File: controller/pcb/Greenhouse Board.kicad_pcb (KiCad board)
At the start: 2 copper layers, 29.1 x 55.5 mm, 9 parts, among them J1 window_control, J2 fan_control, J3 temp_humidity_sensor, J4 misc_sensor_1, J5 misc_sensor_2, Q1 Q_NMOS_GDS, Q2 Q_NMOS_GDS, U1 ESP32-DEVKITC-32D

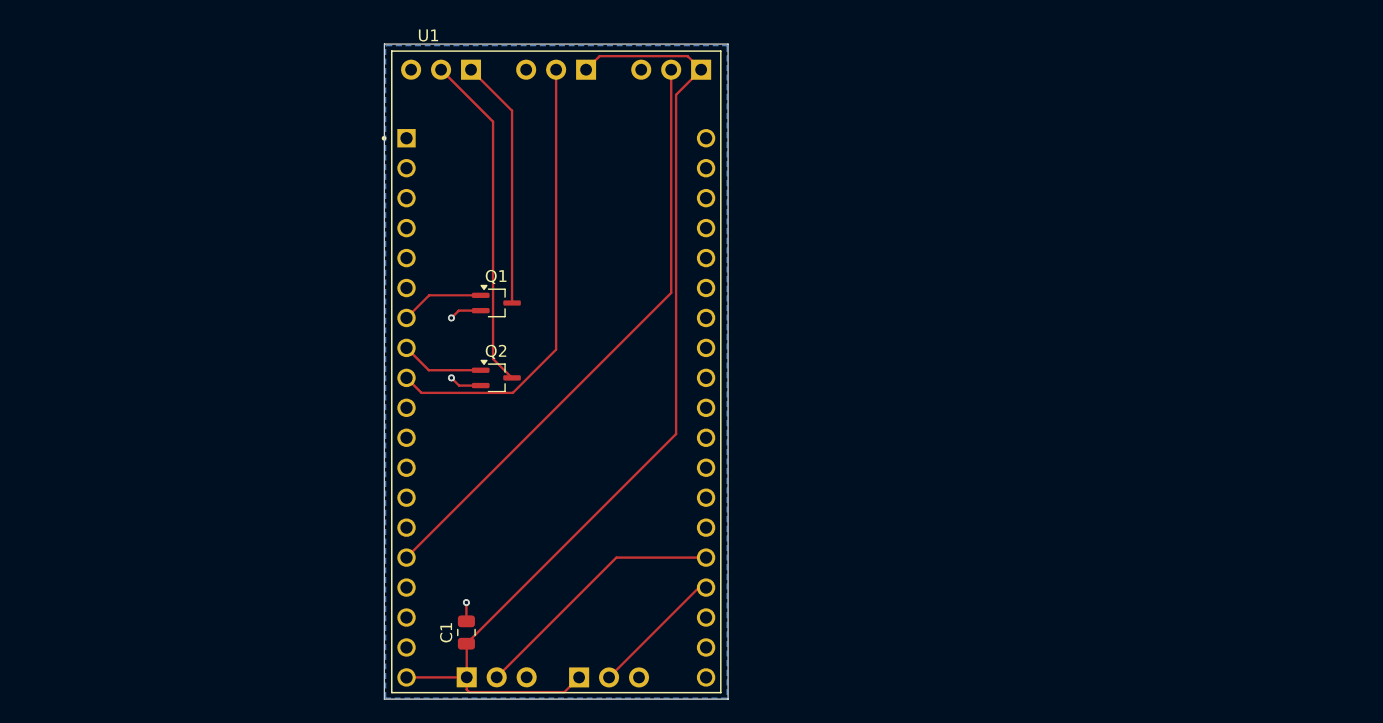
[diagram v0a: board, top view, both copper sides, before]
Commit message: Updates to the PCB to expand its inputs/outputs
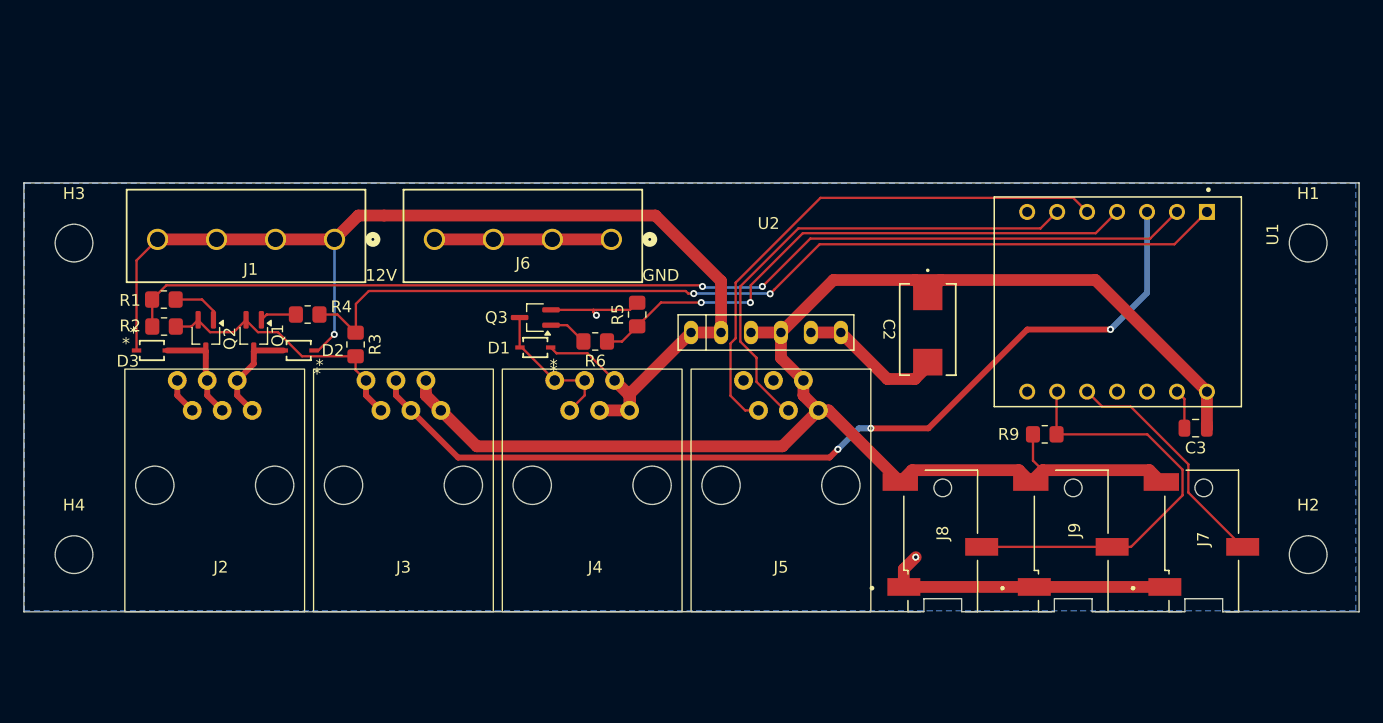
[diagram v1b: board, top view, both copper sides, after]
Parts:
- removed C1: C, Capacitor_SMD:C_0805_2012Metric
- added C2: 220u, Garth:CAP_SP-CAP_SR_PAN, F.Cu at (172.5, 89.9)
- added C3: .1u, Capacitor_SMD:C_0805_2012Metric, F.Cu at (195.2, 98.2)
- added D1: D, Garth:SOD323_DIO, F.Cu at (139.2, 91.4)
- added D2: D, Garth:SOD323_DIO, F.Cu at (119.1, 91.7)
- added D3: D, Garth:SOD323_DIO, F.Cu at (106.7, 91.7)
- added H1: MountingHole, MountingHole:MountingHole_3.2mm_M3, F.Cu at (204.7, 82.5)
- added H2: MountingHole, MountingHole:MountingHole_3.2mm_M3, F.Cu at (204.7, 109.0)
- added H3: MountingHole, MountingHole:MountingHole_3.2mm_M3, F.Cu at (100.1, 82.5)
- added H4: MountingHole, MountingHole:MountingHole_3.2mm_M3, F.Cu at (100.1, 109.0)
- added J6: GND, Garth:screw-terminal-CONN4_TB002-500_787x299_CUD, F.Cu at (145.6, 82.2)
- added J7: T+H sensor, Garth:1_8jack-CUI_SJ2-35853A-SMT-TR, F.Cu at (195.9, 107.8)
- added J8: temp sensor 1, Garth:1_8jack-CUI_SJ2-35853A-SMT-TR, F.Cu at (173.7, 107.8)
- added J9: temp sensor 2, Garth:1_8jack-CUI_SJ2-35853A-SMT-TR, F.Cu at (184.8, 107.8)
- added Q3: Q_NMOS_GDS, Package_TO_SOT_SMD:SOT-323_SC-70_Handsoldering, F.Cu at (139.2, 88.9)
- added R1: 1k, Resistor_SMD:R_0805_2012Metric_Pad1.20x1.40mm_HandSolder, F.Cu at (107.7, 87.3)
- added R2: 100k, Resistor_SMD:R_0805_2012Metric_Pad1.20x1.40mm_HandSolder, F.Cu at (107.7, 89.6)
- added R3: 100k, Resistor_SMD:R_0805_2012Metric_Pad1.20x1.40mm_HandSolder, F.Cu at (124.0, 91.1)
- added R4: 1k, Resistor_SMD:R_0805_2012Metric_Pad1.20x1.40mm_HandSolder, F.Cu at (119.9, 88.6)
- added R5: 100k, Resistor_SMD:R_0805_2012Metric_Pad1.20x1.40mm_HandSolder, F.Cu at (147.8, 88.6)
- added R6: 1k, Resistor_SMD:R_0805_2012Metric_Pad1.20x1.40mm_HandSolder, F.Cu at (144.3, 90.9)
- added R9: 100k, Resistor_SMD:R_0805_2012Metric_Pad1.20x1.40mm_HandSolder, F.Cu at (182.4, 98.8)
- added U2: 12-5V DC/DC, Garth:Power Module 6-pin, F.Cu at (150.5, 92.0)
- J1: value window_control -> 12V; footprint Connector_PinSocket_2.54mm:PinSocket_1x03_P2.54mm_Vertical -> Garth:screw-terminal-CONN4_TB002-500_787x299_CUD; moved to F.Cu
- J2: value fan_control -> window control; footprint Connector_PinSocket_2.54mm:PinSocket_1x03_P2.54mm_Vertical -> Garth:RJ11-RA; moved to F.Cu
- J3: value temp_humidity_sensor -> fan control; footprint Connector_PinSocket_2.54mm:PinSocket_1x03_P2.54mm_Vertical -> Garth:RJ11-RA; moved to F.Cu
- J4: value misc_sensor_1 -> misting control; footprint Connector_PinSocket_2.54mm:PinSocket_1x03_P2.54mm_Vertical -> Garth:RJ11-RA; moved to F.Cu
- J5: value misc_sensor_2 -> light_sensor; footprint Connector_PinSocket_2.54mm:PinSocket_1x03_P2.54mm_Vertical -> Garth:RJ11-RA; moved to F.Cu
- U1: value ESP32-DEVKITC-32D -> XAIO ESP32-C3; footprint ESP32-DEVKITC-32D:MODULE_ESP32-DEVKITC-32D -> Garth:MODULE_113991054
- moved U1 48.0 mm to (188.6, 87.5), turned to -90 degrees
- moved J2 42.7 mm to (112.0, 96.7), turned to 180 degrees
- moved J3 38.4 mm to (128.0, 96.7), turned to 180 degrees
- moved J5 28.4 mm to (160.0, 96.7), turned to 180 degrees
- moved J4 25.0 mm to (144.0, 96.7), turned to 180 degrees
- moved Q2 24.9 mm to (111.3, 90.4), turned to -90 degrees
- moved Q1 20.8 mm to (115.3, 90.4), turned to -90 degrees
- moved J1 18.5 mm to (122.2, 82.2), turned to 0 degrees
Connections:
- J1 pad 1: /green_wire -> +12V
- J1 pad 2: /red_wire -> +12V
- J1 pad 3: GND -> +12V
- J2 pad 1: +5V -> /green_wire
- J2 pad 2: /fan_signal -> /green_wire
- J2 pad 3: GND -> /red_wire
- J3 pad 2: /temp_data -> +5V
- J3 pad 3: GND -> /fan_signal
- J4 pad 1: +5V -> +12V
- J4 pad 2: /misc_data1 -> +12V
- J4 pad 3: GND -> +12V
- J5 pad 2: /misc_data2 -> +5V
- J5 pad 3: GND -> /SCL
- Q1 pad 1: /window_close -> Net-(Q1-G)
- Q2 pad 1: /window_open -> Net-(Q2-G)
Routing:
- net +12V: track 0.00 -> 99.3 mm, vias 0 -> 1
- net /window_open: track 7.07 -> 92.4 mm, vias 0 -> 2
- net GND: track 7.08 -> 90.3 mm, vias 3 -> 2
- net /window_close: track 7.09 -> 81.8 mm, vias 0 -> 2
- net /temp_data: track 50.7 -> 0.00 mm
- net /mist_control: track 0.00 -> 48.6 mm, vias 0 -> 2
- net +5V: track 86.8 -> 133.1 mm
- net /SDA: track 0.00 -> 45.9 mm
- net /SCL: track 0.00 -> 41.9 mm
- net /fan_signal: track 38.5 -> 79.8 mm, vias 0 -> 3
- net /temp_bus: track 0.00 -> 36.6 mm
- net /misc_data1: track 22.0 -> 0.00 mm
- net /DHT22_Sensor: track 0.00 -> 20.0 mm
- net /red_wire: track 28.6 -> 8.89 mm
- net /green_wire: track 21.2 -> 8.66 mm
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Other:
- board size 29.1 x 55.5 mm -> 113.2 x 36.4 mm
- board text added: "12V"
- board text added: "Greenhouse Controller v2.0 2025-04-16"
- board text added: "SCL"
- board text added: "SDA"
- board text added: "T+H"
- board text added: "fan"
- board text added: "fan control"
- board text added: "green"
- board text added: "light sensor"
- board text added: "mist control"
- board text added: "mist-"
- board text added: "red"
- board text added: "temp1"
- board text added: "temp2"
- board text added: "window control"
- board text removed: "DAT"
- board text removed: "DAT1"
- board text removed: "DAT2"
- board text removed: "G"
- board text removed: "Greenhouse Controller v1.0 2024-05-19"
- board text removed: "R"
- board text removed: "SIG"
